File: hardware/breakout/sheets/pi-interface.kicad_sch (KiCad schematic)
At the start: 25 parts, among them J10 Barcode spare 1, J11 Barcode spare 2, J12 Barcode spare 3, J13 Dual panel BNC: Eye camera tr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, J15 Dual panel BNC: Behavior came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, J17 Dual panel BNC: Behavior came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, J18 Internal USB-A (sync-module p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, J7 Sync-module 40-pin GPIO heade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, J8 Barcode -> NI optocoupler (Ta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, J9 Barcode -> Intan optocoupler 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, U14 SN74LVC541APW, U15 SN74AHCT541PW, U74 SN74AHCT541PW

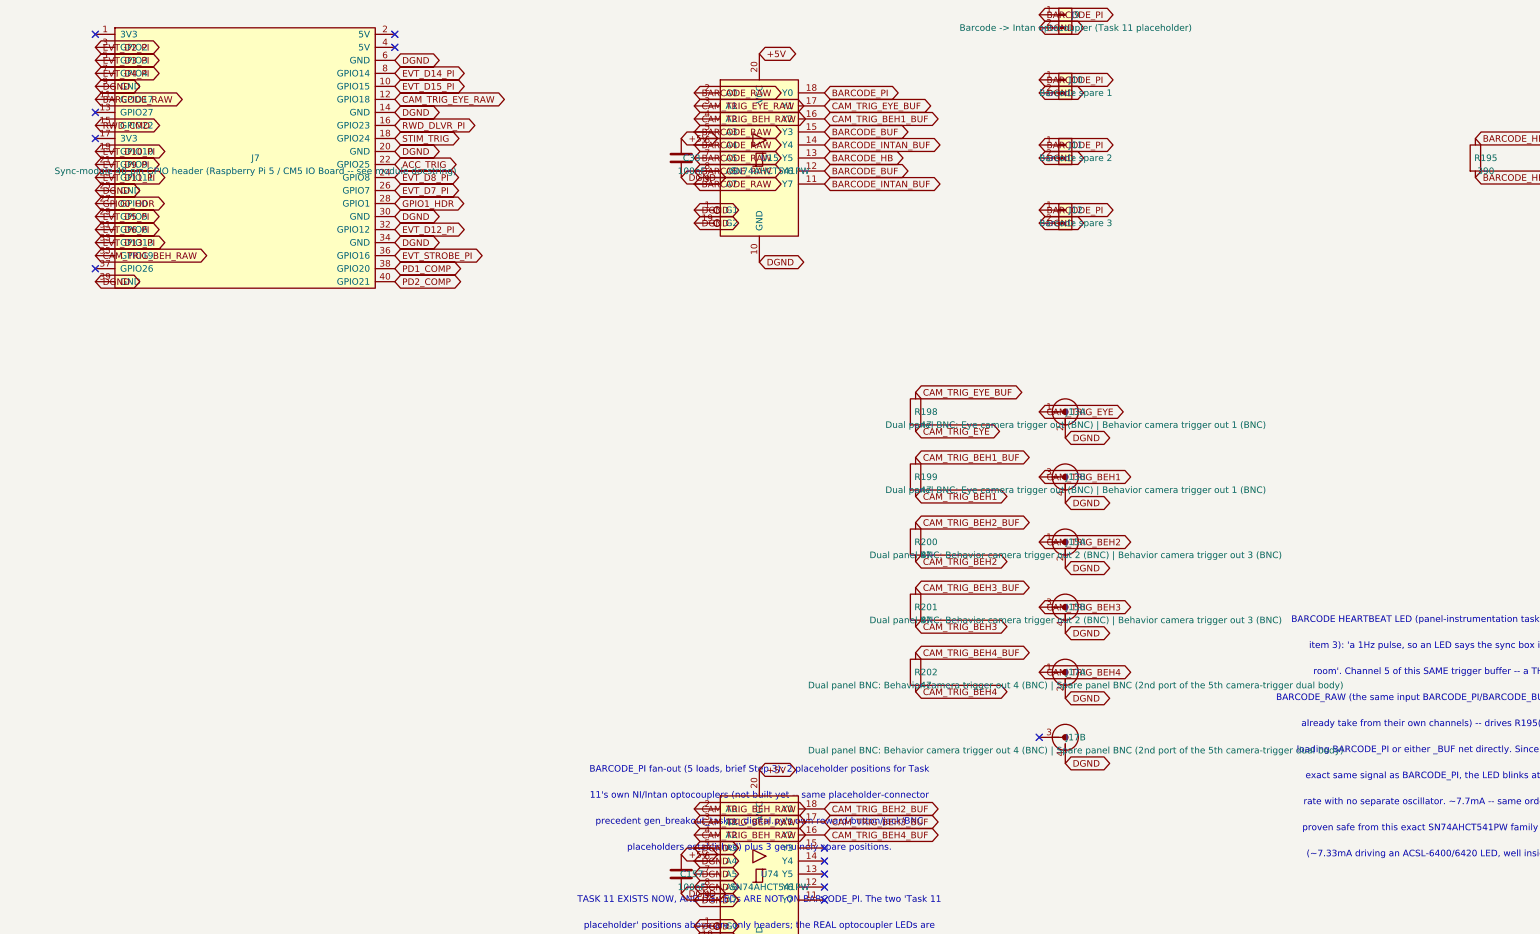
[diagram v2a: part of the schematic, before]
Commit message: feat(hardware): camera lines carry the barcode, not a trigger
The cameras free-run, so this box does not clock them -- they need a shared
TIMEBASE they can record, which is what the barcode already is. The five
camera-facing panel BNCs now carry BARCODE_RAW instead of the hardware-PWM
triggers from GPIO18/19.

It costs nothing on the board. Same buffers, same 47 ohm series resistors, same
five BNCs, same panel: only the INPUT NET of five buffer channels moved
(U15.A3/A4 and U74.A2/A3/A4). No new parts, no new panel holes, no refdes
disturbed. Nets renamed CAM_TRIG_* -> CAM_SYNC_*, because the old names describe
a clock those lines no longer carry, and a name that is right about the model and
wrong about the board is this project's recurring failure.

GPIO18 and GPIO19 become spare and are no-connected, so the board now has four
spare GPIOs instead of two, and two of the four are hardware-PWM capable.

THE CONSEQUENCE IS BIGGER THAN THE CHANGE, and is why doing it in design phase
was worth it. Spec Sec.4 justifies the PIO capture window starting at GPIO0 on
the grounds that "camera triggers must land on a hardware PWM pin (12, 13, 18,
19)... only the window starting at 2 leaves even one PWM pin free -- insufficient
for two triggers." No camera line needs a PWM pin now, so that constraint has
expired. GPIO0/1 are in the capture window ONLY because it had to start at 0, and
they are the two pins the Pi probes as I2C at boot for a HAT ID EEPROM -- which
is why they carry 330 ohm series resistors and need force_eeprom_read=0. Moving
the window to GPIO2-18 would delete that whole mitigation and free two more pins.

NOT DONE, deliberately: it re-maps 17 event lines across two sheets and the board
works as it stands. Recorded in hardware/breakout/camera-sync-change.md so that
nobody later reads spec Sec.4's justification without knowing it no longer holds.

What this does NOT solve, also recorded: frame times are no longer known by
construction, so spec Sec.12 item 1's just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
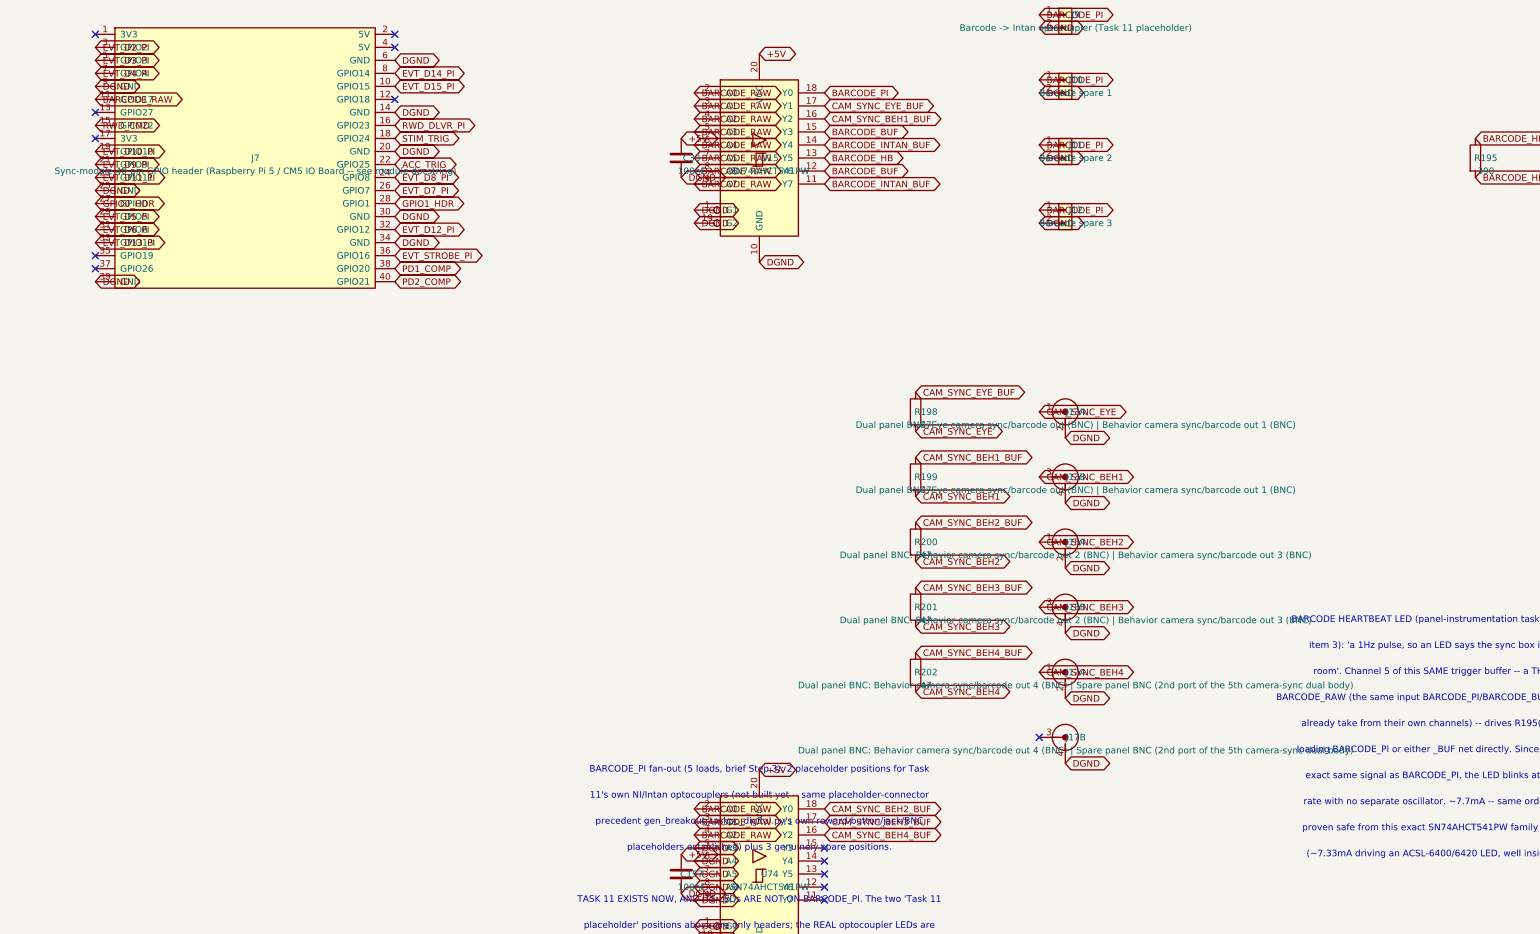
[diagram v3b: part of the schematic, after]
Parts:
- J13: value Dual panel BNC: Eye camera trigger out (BNC) | Behavior camera trigger out 1 (BNC) -> Dual panel BNC: Eye camera sync/barcode out (BNC) | Behavior camera sync/barcode out 1 (BNC)
- J15: value Dual panel BNC: Behavior camera trigger out 2 (BNC) | Behavior camera trigger out 3 (BNC) -> Dual panel BNC: Behavior camera sync/barcode out 2 (BNC) | Behavior camera sync/barcode out 3 (BNC)
- J17: value Dual panel BNC: Behavior camera trigger out 4 (BNC) | Spare panel BNC (2nd port of the 5th camera-trigger dual body) -> Dual panel BNC: Behavior camera sync/barcode out 4 (BNC) | Spare panel BNC (2nd port of the 5th camera-sync dual body)
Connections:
- net BARCODE_RAW: now also U15.3 (A1), U15.4 (A2), U74.2 (A0), U74.3 (A1), U74.4 (A2)
- net CAM_TRIG_BEH1 renamed CAM_SYNC_BEH1
- net CAM_TRIG_BEH1_BUF renamed CAM_SYNC_BEH1_BUF
- net CAM_TRIG_BEH2 renamed CAM_SYNC_BEH2
- net CAM_TRIG_BEH2_BUF renamed CAM_SYNC_BEH2_BUF
- net CAM_TRIG_BEH3 renamed CAM_SYNC_BEH3
- net CAM_TRIG_BEH3_BUF renamed CAM_SYNC_BEH3_BUF
- net CAM_TRIG_BEH4 renamed CAM_SYNC_BEH4
- net CAM_TRIG_BEH4_BUF renamed CAM_SYNC_BEH4_BUF
- removed net CAM_TRIG_BEH_RAW: J7.35 (GPIO19), U15.4 (A2), U74.2 (A0), U74.3 (A1), U74.4 (A2)
- net CAM_TRIG_EYE renamed CAM_SYNC_EYE
- net CAM_TRIG_EYE_BUF renamed CAM_SYNC_EYE_BUF
- net CAM_TRIG_EYE_RAW: no longer names the net of J7.12 (GPIO18)
- net CAM_TRIG_EYE_RAW: no longer U15.3 (A1)
- no-connect marks 19 -> 21
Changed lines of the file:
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@@
 		)
 	)
-	(global_label "CAM_TRIG_EYE_RAW"
-		(shape bidirectional)
-		(at 228.6 148.59 0)
-		(effects (font (size 1.27 1.27)) (justify left))
-		(property "Intersheetrefs" "${INTERSHEET_REFS}"
-			(at 228.6 148.59 0)
-			(effects (font (size 1.27 1.27)) (hide yes))
-		)
-	)
-	(global_label "CAM_TRIG_BEH_RAW"
-		(shape bidirectional)
-		(at 170.17999999999998 179.07000000000002 0)
-		(effects (font (size 1.27 1.27)) (justify left))
-		(property "Intersheetrefs" "${INTERSHEET_REFS}"
-			(at 170.17999999999998 179.07000000000002 0)
-			(effects (font (size 1.27 1.27)) (hide yes))
-		)
+	(no_connect
+		(at 228.6 148.59)
+	)
+	(no_connect
+		(at 170.17999999999998 179.07000000000002)
 	)
 	(global_label "PD1_COMP"
@@
 		)
 	)
-	(global_label "CAM_TRIG_EYE_RAW"
+	(global_label "BARCODE_RAW"
 		(shape bidirectional)
 		(at 287.02000000000004 149.86 0)
@@
 		)
 	)
-	(global_label "CAM_TRIG_EYE_BUF"
+	(global_label "CAM_SYNC_EYE_BUF"
 		(shape bidirectional)
 		(at 312.42 149.86 0)
@@
 		)
 	)
-	(global_label "CAM_TRIG_BEH_RAW"
+	(global_label "BARCODE_RAW"
 		(shape bidirectional)
 		(at 287.02000000000004 152.4 0)
@@
 		)
 	)
-	(global_label "CAM_TRIG_BEH1_BUF"
+	(global_label "CAM_SYNC_BEH1_BUF"
 		(shape bidirectional)
 		(at 312.42 152.4 0)
@@
 		)
 	)
-	(global_label "CAM_TRIG_EYE_BUF"
+	(global_label "CAM_SYNC_EYE_BUF"
 		(shape bidirectional)
 		(at 330.2 205.74 0)
@@
 		)
 	)
-	(global_label "CAM_TRIG_EYE"
+	(global_label "CAM_SYNC_EYE"
 		(shape bidirectional)
 		(at 330.2 213.36 0)
@@
 			(effects (font (size 1.27 1.27)))
 		)
-		(property "Value" "Dual panel BNC: Eye camera trigger out (BNC) | Behavior camera trigger out 1 (BNC)"
+		(property "Value" "Dual panel BNC: Eye camera sync/barcode out (BNC) | Behavior camera sync/barcode out 1 (BNC)"
 			(at 361.442 212.09 0)
 			(effects (font (size 1.27 1.27)))
@@
 		)
 	)
-	(global_label "CAM_TRIG_EYE"
+	(global_label "CAM_SYNC_EYE"
 		(shape bidirectional)
 		(at 354.33000000000004 209.55 0)
@@
 		)
 	)
-	(global_label "CAM_TRIG_BEH1_BUF"
+	(global_label "CAM_SYNC_BEH1_BUF"
 		(shape bidirectional)
 		(at 330.2 218.44 0)
@@
 		)
 	)
-	(global_label "CAM_TRIG_BEH1"
+	(global_label "CAM_SYNC_BEH1"
 		(shape bidirectional)
 		(at 330.2 226.06 0)
@@
 			(effects (font (size 1.27 1.27)))
 		)
-		(property "Value" "Dual panel BNC: Eye camera trigger out (BNC) | Behavior camera trigger out 1 (BNC)"
+		(property "Value" "Dual panel BNC: Eye camera sync/barcode out (BNC) | Behavior camera sync/barcode out 1 (BNC)"
 			(at 361.442 224.79 0)
 			(effects (font (size 1.27 1.27)))
@@
 		)
 	)
-	(global_label "CAM_TRIG_BEH1"
+	(global_label "CAM_SYNC_BEH1"
 		(shape bidirectional)
 		(at 354.33000000000004 222.25 0)
@@
 		)
 	)
-	(global_label "CAM_TRIG_BEH2_BUF"
+	(global_label "CAM_SYNC_BEH2_BUF"
 		(shape bidirectional)
 		(at 330.2 231.14000000000001 0)
@@
 		)
 	)
-	(global_label "CAM_TRIG_BEH2"
+	(global_label "CAM_SYNC_BEH2"
 		(shape bidirectional)
 		(at 330.2 238.76000000000002 0)
@@
 			(effects (font (size 1.27 1.27)))
 		)
-		(property "Value" "Dual panel BNC: Behavior camera trigger out 2 (BNC) | Behavior camera trigger out 3 (BNC)"
+		(property "Value" "Dual panel BNC: Behavior camera sync/barcode out 2 (BNC) | Behavior camera sync/barcode out 3 (BNC)"
 			(at 361.442 237.49 0)
 			(effects (font (size 1.27 1.27)))
@@
 		)
 	)
-	(global_label "CAM_TRIG_BEH2"
+	(global_label "CAM_SYNC_BEH2"
 		(shape bidirectional)
 		(at 354.33000000000004 234.95000000000002 0)
@@
 		)
 	)
-	(global_label "CAM_TRIG_BEH3_BUF"
+	(global_label "CAM_SYNC_BEH3_BUF"
 		(shape bidirectional)
 		(at 330.2 243.84 0)
@@
 		)
 	)
-	(global_label "CAM_TRIG_BEH3"
+	(global_label "CAM_SYNC_BEH3"
 		(shape bidirectional)
 		(at 330.2 251.46 0)
@@
 			(effects (font (size 1.27 1.27)))
 		)
-		(property "Value" "Dual panel BNC: Behavior camera trigger out 2 (BNC) | Behavior camera trigger out 3 (BNC)"
+		(property "Value" "Dual panel BNC: Behavior camera sync/barcode out 2 (BNC) | Behavior camera sync/barcode out 3 (BNC)"
 			(at 361.442 250.19 0)
 			(effects (font (size 1.27 1.27)))
@@
 		)
 	)
-	(global_label "CAM_TRIG_BEH3"
+	(global_label "CAM_SYNC_BEH3"
 		(shape bidirectional)
 		(at 354.33000000000004 247.65 0)
@@
 		)
 	)
-	(global_label "CAM_TRIG_BEH4_BUF"
+	(global_label "CAM_SYNC_BEH4_BUF"
 		(shape bidirectional)
 		(at 330.2 256.54 0)
@@
 		)
 	)
-	(global_label "CAM_TRIG_BEH4"
+	(global_label "CAM_SYNC_BEH4"
 		(shape bidirectional)
 		(at 330.2 264.16 0)
@@
 			(effects (font (size 1.27 1.27)))
 		)
-		(property "Value" "Dual panel BNC: Behavior camera trigger out 4 (BNC) | Spare panel BNC (2nd port of the 5th camera-trigger dual body)"
+		(property "Value" "Dual panel BNC: Behavior camera sync/barcode out 4 (BNC) | Spare panel BNC (2nd port of the 5th camera-sync dual body)"
 			(at 361.442 262.89000000000004 0)
 			(effects (font (size 1.27 1.27)))
@@
 		)
 	)
-	(global_label "CAM_TRIG_BEH4"
+	(global_label "CAM_SYNC_BEH4"
 		(shape bidirectional)
 		(at 354.33000000000004 260.35 0)
@@
 			(effects (font (size 1.27 1.27)))
 		)
-		(property "Value" "Dual panel BNC: Behavior camera trigger out 4 (BNC) | Spare panel BNC (2nd port of the 5th camera-trigger dual body)"
+		(property "Value" "Dual panel BNC: Behavior camera sync/barcode out 4 (BNC) | Spare panel BNC (2nd port of the 5th camera-sync dual body)"
 			(at 361.442 275.59000000000003 0)
 			(effects (font (size 1.27 1.27)))
@@
 		)
 	)
-	(global_label "CAM_TRIG_BEH_RAW"
+	(global_label "BARCODE_RAW"
 		(shape bidirectional)
 		(at 287.02000000000004 287.02000000000004 0)
@@
 		)
 	)
-	(global_label "CAM_TRIG_BEH2_BUF"
+	(global_label "CAM_SYNC_BEH2_BUF"
 		(shape bidirectional)
 		(at 312.42 287.02000000000004 0)
@@
 		)
 	)
-	(global_label "CAM_TRIG_BEH_RAW"
+	(global_label "BARCODE_RAW"
 		(shape bidirectional)
 		(at 287.02000000000004 289.56 0)
@@
 		)
 	)
-	(global_label "CAM_TRIG_BEH3_BUF"
+	(global_label "CAM_SYNC_BEH3_BUF"
 		(shape bidirectional)
 		(at 312.42 289.56 0)
@@
 		)
 	)
-	(global_label "CAM_TRIG_BEH_RAW"
+	(global_label "BARCODE_RAW"
 		(shape bidirectional)
 		(at 287.02000000000004 292.1 0)
@@
 		)
 	)
-	(global_label "CAM_TRIG_BEH4_BUF"
+	(global_label "CAM_SYNC_BEH4_BUF"
 		(shape bidirectional)
 		(at 312.42 292.1 0)
